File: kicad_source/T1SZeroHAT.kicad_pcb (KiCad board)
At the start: 2 copper layers, 65 x 30 mm, 45 parts, among them CN1 RASPI-IO, CN2 XY2500R-F-3.81-2P, CN3 SM02B-GHS-TB, CN4 SM02B-GHS-TB, SW1 SS-3235S-L3, U1 LAN8651, Y1 X1E0000210808

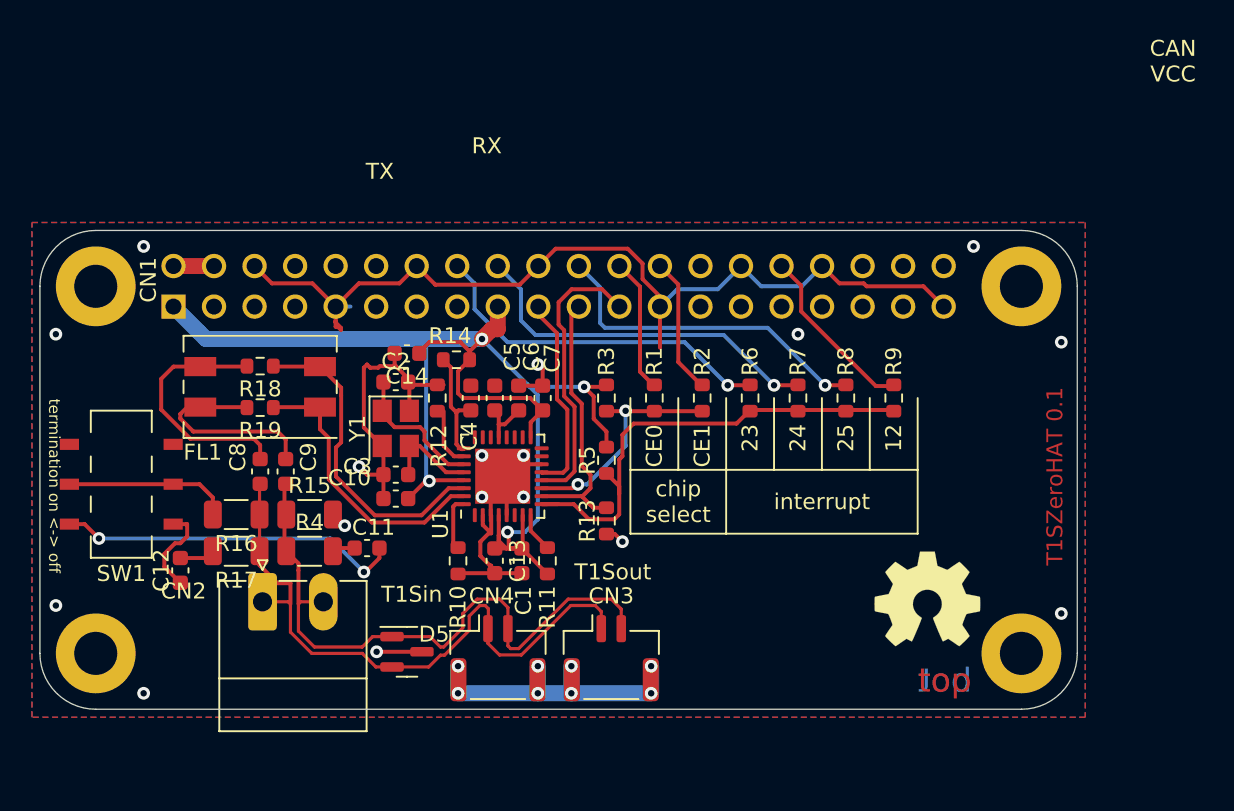
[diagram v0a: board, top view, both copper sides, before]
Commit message: corrected common mode choke and added part number
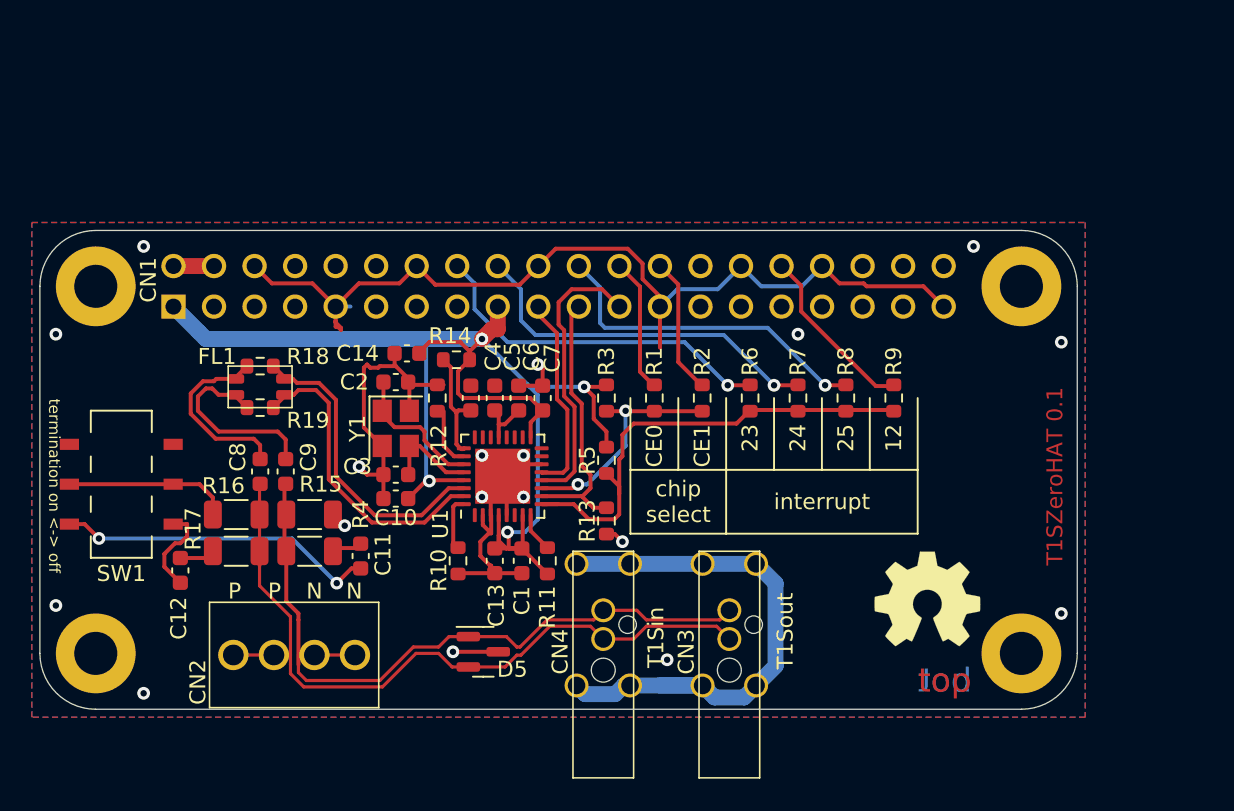
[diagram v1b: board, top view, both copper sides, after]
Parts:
- CN2: value XY2500R-F-3.81-2P -> WE_691210910004; footprint Connector_Phoenix_MC:PhoenixContact_MC_1,5_2-G-3.81_1x02_P3.81mm_Horizontal -> generationmake:WE_691210910004
- CN3, CN4: value SM02B-GHS-TB -> SPE-T1-STRM-90; footprint Connector_JST:JST_GH_SM02B-GHS-TB_1x02-1MP_P1.25mm_Horizontal -> generationmake:SPE-T1-STRM-90
- FL1: value Filter_EMI_CommonMode -> ACT1210D-131-2P-TL00; footprint Filter:Filter_Bourns_SRF0905_6.0x9.2mm -> generationmake:TDK_ACT1210D
- moved CN3 10.5 mm to (150.7, 120.8), turned to 90 degrees
- moved CN4 9.99 mm to (142.8, 120.8), turned to 90 degrees
- moved D5 4.78 mm to (135.3, 112.9)
- moved CN2 3.88 mm to (123.4, 113.1)
- moved C11 0.64 mm to (127.6, 106.9), turned to -90 degrees
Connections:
- CN2 pad 2: /TRXN -> /TRXP
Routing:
- net /MP: track 18.9 -> 34.9 mm, vias 8 -> 0
- net /TRXP: track 40.0 -> 48.3 mm
- net /TRXN: track 39.9 -> 46.7 mm
- net /TRXP_I: track 15.6 -> 11.6 mm
- net /TRXN_C: track 18.0 -> 19.4 mm
- net Net-(SW1A-A): track 21.7 -> 20.3 mm
- net /TRXP_C: track 20.2 -> 19.4 mm
- net /TRXN_I: track 13.0 -> 12.2 mm
- net GND: vias 17 -> 18
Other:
- board text added: "Licensed under CERN-OHL-W v2"
- board text added: "N"
- board text added: "P"
- board text removed: "CAN VCC"
- board text removed: "Licensed under CERN OHL v.1.2"
- board text removed: "RX"
- board text removed: "TX"

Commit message: updated schematic pdf
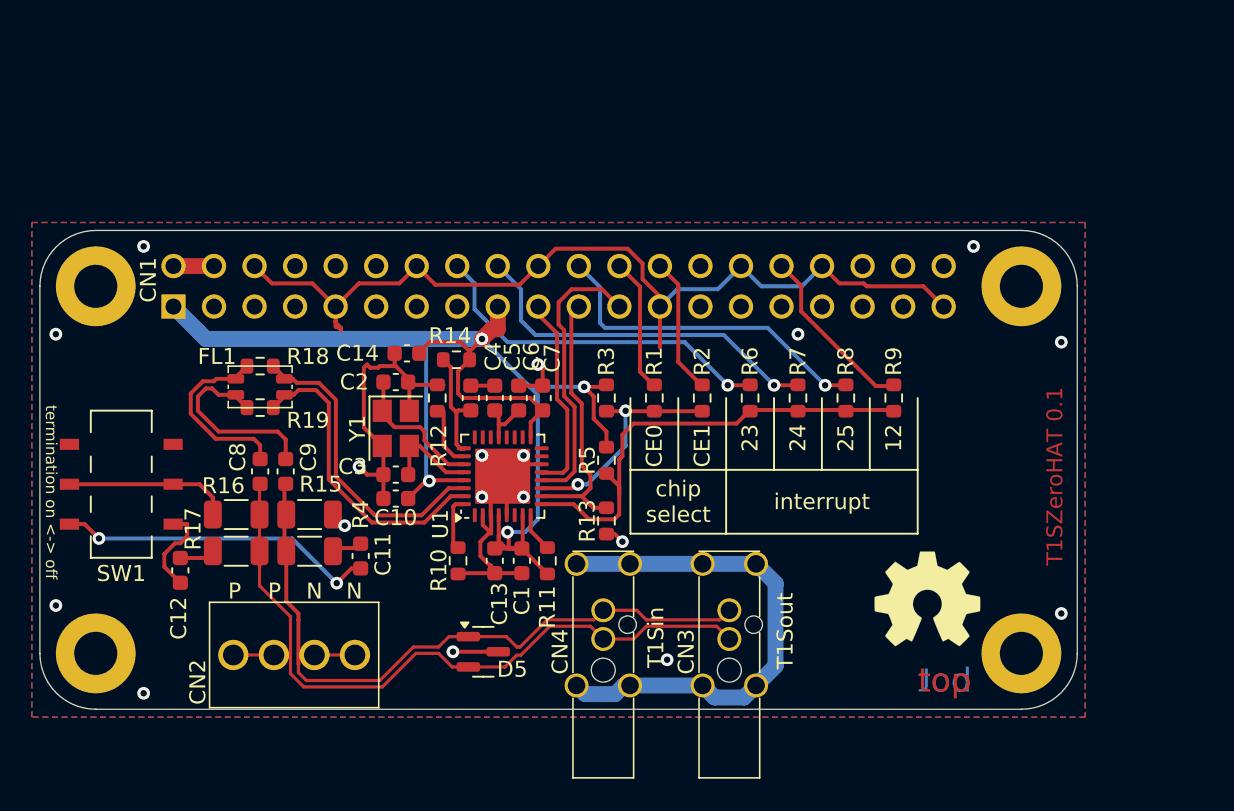
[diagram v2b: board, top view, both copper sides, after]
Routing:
- net /MP: track 34.9 -> 32.2 mm
- net /LAN8651_INT: track 30.7 -> 29.7 mm
- net GND: track 113.7 -> 114.2 mm

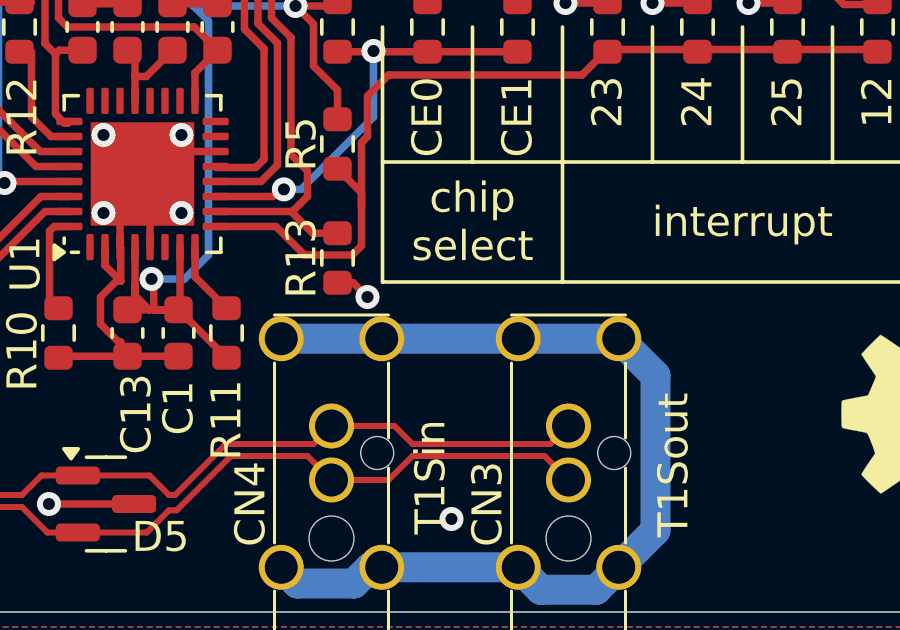
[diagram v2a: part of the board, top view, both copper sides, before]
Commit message: fixed some DRCs
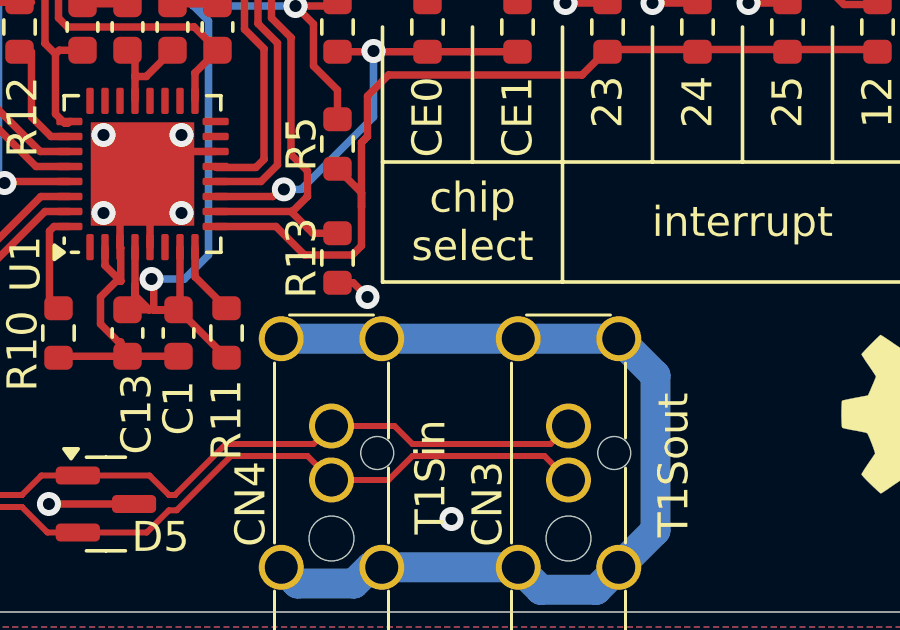
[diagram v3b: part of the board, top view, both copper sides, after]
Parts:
- CN1: footprint MODULE_compute:RASPI_ZERO_HAT_EDGE -> generationmake:RASPI_ZERO_HAT_EDGE
- L1: footprint labels:generationmake_small_solder -> generationmake:generationmake_small_solder
- L2: footprint labels:generationmake_logo -> generationmake:generationmake_logo
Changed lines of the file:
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@@
 		(attr through_hole)
 		(fp_line
-			(start 14.2 -1.9)
-			(end 14.2 1.9)
+			(start 6.6 -1.9)
+			(end 12.6 -1.9)
 			(stroke
 				(width 0.1)
@@
 		)
 		(fp_line
-			(start 6.6 -1.9)
-			(end 12.6 -1.9)
+			(start 0 -1.9)
+			(end 5 -1.9)
 			(stroke
 				(width 0.1)
@@
 		)
 		(fp_line
-			(start 0 -1.9)
-			(end 5 -1.9)
+			(start 14.2 -1.4)
+			(end 14.2 1.4)
 			(stroke
 				(width 0.1)
@@
 		(attr through_hole)
 		(fp_line
-			(start 14.2 -1.9)
-			(end 14.2 1.9)
+			(start 6.6 -1.9)
+			(end 12.6 -1.9)
 			(stroke
 				(width 0.1)
@@
 		)
 		(fp_line
-			(start 6.6 -1.9)
-			(end 12.6 -1.9)
+			(start 0 -1.9)
+			(end 5 -1.9)
 			(stroke
 				(width 0.1)
@@
 		)
 		(fp_line
-			(start 0 -1.9)
-			(end 5 -1.9)
+			(start 14.2 -1.4)
+			(end 14.2 1.4)
 			(stroke
 				(width 0.1)
@@
 		)
 	)
-	(footprint "labels:generationmake_small_solder"
+	(footprint "generationmake:generationmake_small_solder"
 		(layer "F.Cu")
 		(at 170.7 102 90)
@@
 			)
 		)
-		(property "Footprint" "labels:generationmake_small_solder"
+		(property "Footprint" "generationmake:generationmake_small_solder"
 			(at 0 0 90)
 			(layer "F.Fab")
@@
 			)
 		)
-		(property "exclude_from_bom" ""
-			(at 272.7 -68.7 0)
-			(layer "F.Fab")
-			(hide yes)
-			(effects
-				(font
-					(size 1 1)
-					(thickness 0.15)
-				)
-			)
-		)
 		(sheetname "Stammblatt")
 		(sheetfile "T1SZeroHAT.kicad_sch")
@@
 		)
 	)
-	(footprint "MODULE_compute:RASPI_ZERO_HAT_EDGE"
+	(footprint "generationmake:RASPI_ZERO_HAT_EDGE"
 		(locked yes)
 		(layer "F.Cu")
@@
 			)
 		)
-		(property "Footprint" "MODULE_compute:RASPI_ZERO_HAT_EDGE"
+		(property "Footprint" "generationmake:RASPI_ZERO_HAT_EDGE"
 			(at 0 0 0)
 			(layer "F.Fab")
@@
 		(property "Footprint" "Symbol:OSHW-Symbol_6.7x6mm_SilkScreen"
 			(at 0 0 0)
+			(unlocked yes)
 			(layer "F.Fab")
 			(hide yes)
@@
 		(property "Datasheet" ""
 			(at 0 0 0)
+			(unlocked yes)
 			(layer "F.Fab")
 			(hide yes)
@@
 		(property "Description" ""
 			(at 0 0 0)
+			(unlocked yes)
 			(layer "F.Fab")
 			(hide yes)
@@
 		(sheetname "Stammblatt")
 		(sheetfile "T1SZeroHAT.kicad_sch")
-		(attr exclude_from_pos_files exclude_from_bom)
+		(attr exclude_from_pos_files exclude_from_bom allow_missing_courtyard)
 		(fp_poly
 			(pts
@@
 		)
 	)
-	(footprint "labels:generationmake_logo"
+	(footprint "generationmake:generationmake_logo"
 		(layer "B.Cu")
 		(at 140 104 180)
@@
 			)
 		)
-		(property "Footprint" "labels:generationmake_logo"
-			(at 0 0 180)
-			(layer "F.Fab")
+		(property "Footprint" "generationmake:generationmake_logo"
+			(at 0 0 0)
+			(layer "B.Fab")
 			(hide yes)
 			(effects
@@
 					(thickness 0.15)
 				)
+				(justify mirror)
 			)
 		)
 		(property "Datasheet" ""
-			(at 0 0 180)
-			(layer "F.Fab")
+			(at 0 0 0)
+			(layer "B.Fab")
 			(hide yes)
 			(effects
@@
 					(thickness 0.15)
 				)
+				(justify mirror)
 			)
 		)
 		(property "Description" ""
-			(at 0 0 180)
-			(layer "F.Fab")
-			(hide yes)
-			(effects
-				(font
-					(size 1.27 1.27)
-					(thickness 0.15)
-				)
-			)
-		)
-		(property "exclude_from_bom" ""
-			(at 280 208 0)
+			(at 0 0 0)
 			(layer "B.Fab")
 			(hide yes)
 			(effects
 				(font
-					(size 1 1)
+					(size 1.27 1.27)
 					(thickness 0.15)
 				)
